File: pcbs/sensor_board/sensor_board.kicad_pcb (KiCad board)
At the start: 2 copper layers, 32 x 51 mm, 49 parts, among them J1 1.5mm, J2 2.5mm, J3 2.5mm, J4 1.5 mm, J5 RJ45, J6 Conn_01x06, J7 Conn_01x02, J8 Conn_01x02, Q1 220mA / 50V, Q2 220mA / 50V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

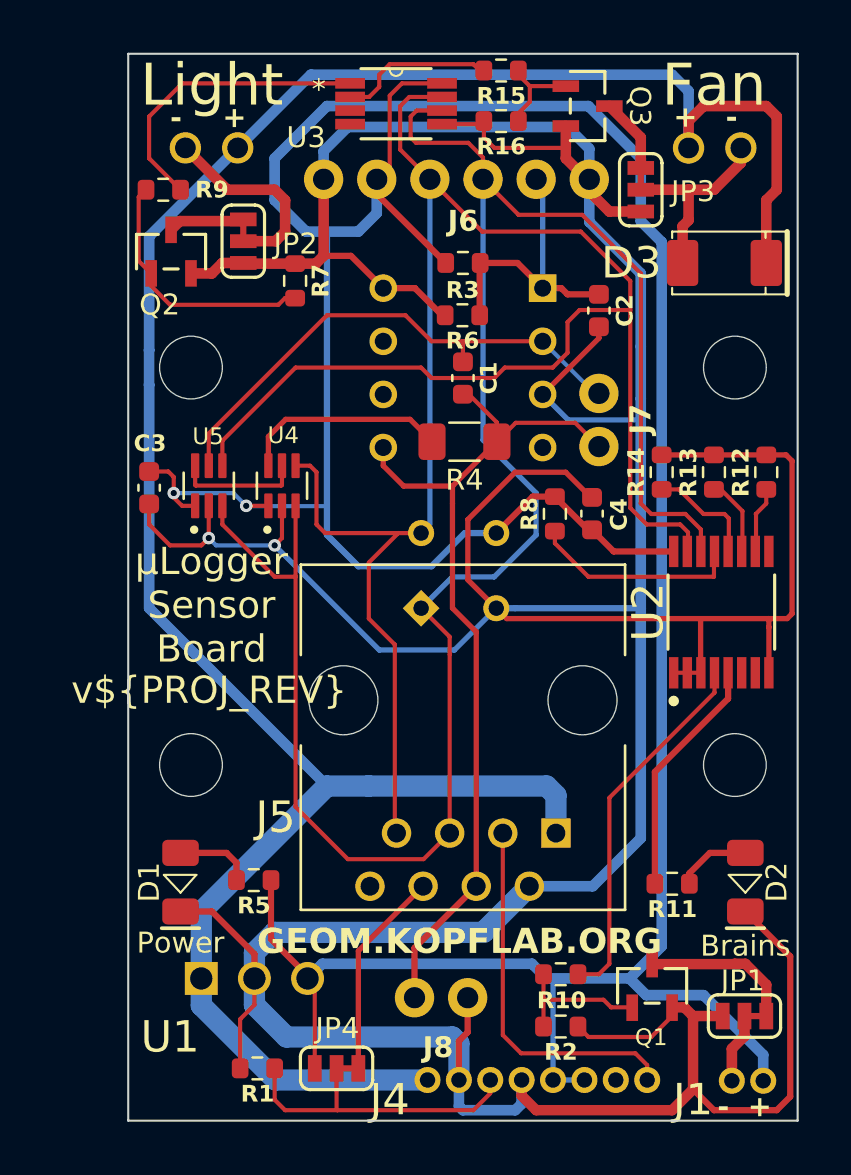
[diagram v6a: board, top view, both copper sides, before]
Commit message: update sensor board with 1M potentiometer
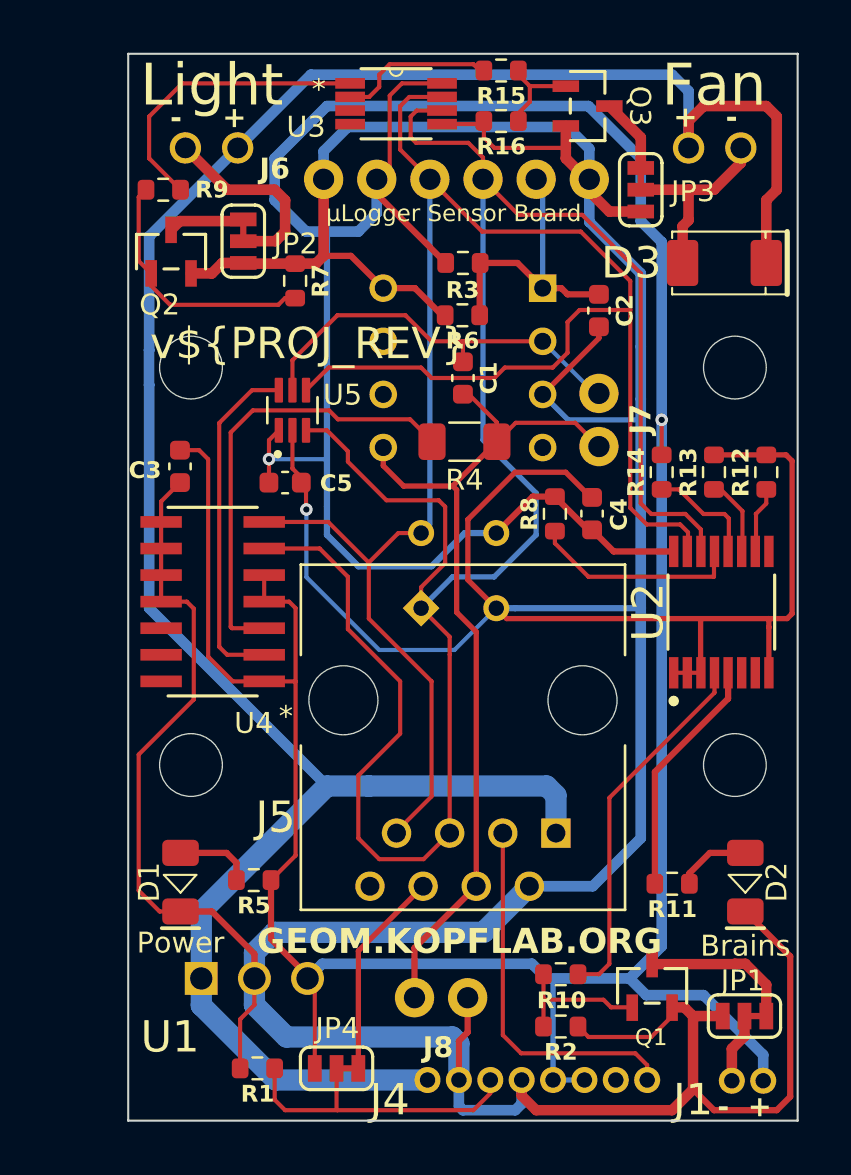
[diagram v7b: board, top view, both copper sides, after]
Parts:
- added C5: 100nF, footprints:C_0603, F.Cu at (140.0, 100.0)
- U4: value 100 kOhm -> 1 MOhm; footprint footprints:SOT-363_TSSOP6_SC88 -> footprints:14-SOIC
- moved U4 6.46 mm to (136.5, 105.7), turned to 180 degrees
- moved U5 5.39 mm to (140.3, 96.5)
- moved C3 1.79 mm to (135.0, 99.2)
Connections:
- R14 pad 2: GND -> +5V
- R4 pad 2: Net-(U4-B) -> Net-(U4-B1)
- U4 pad 2: GND -> Net-(U4-W1)
- U4 pad 3: /SCL -> Net-(U4-B1)
- U4 pad 4: /SDA -> +5V
- U4 pad 5: Net-(U4-W) -> +5V
- U4 pad 6: Net-(U4-B) -> /SCL
- U5 pad 6: Net-(U4-W) -> Net-(U4-W1)
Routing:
- net +5V: track 169.6 -> 196.4 mm
- net Net-(U4-B1): track 0.00 -> 21.5 mm
- net Net-(U4-W1): track 0.00 -> 16.5 mm
- net GND: track 261.4 -> 277.3 mm, vias 2 -> 1
- net Net-(U4-B): track 9.94 -> 0.00 mm
- net /SCL: track 97.4 -> 106.7 mm
- net /SDA: track 98.5 -> 91.9 mm
- net Net-(U4-W): track 6.02 -> 0.00 mm
- net /AMP: track 25.1 -> 19.5 mm
